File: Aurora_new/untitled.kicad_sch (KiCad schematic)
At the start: 18 parts, among them U15 MCP1826S-5002E/DB, U16 MCP1826S-5002E/DB, U17 MCP1826ST-3302E/DB, U18 MCP1826ST-3302E/DB, U19 MCP1826ST-3302E/DB, U4 MCP1826S-5002E/DB

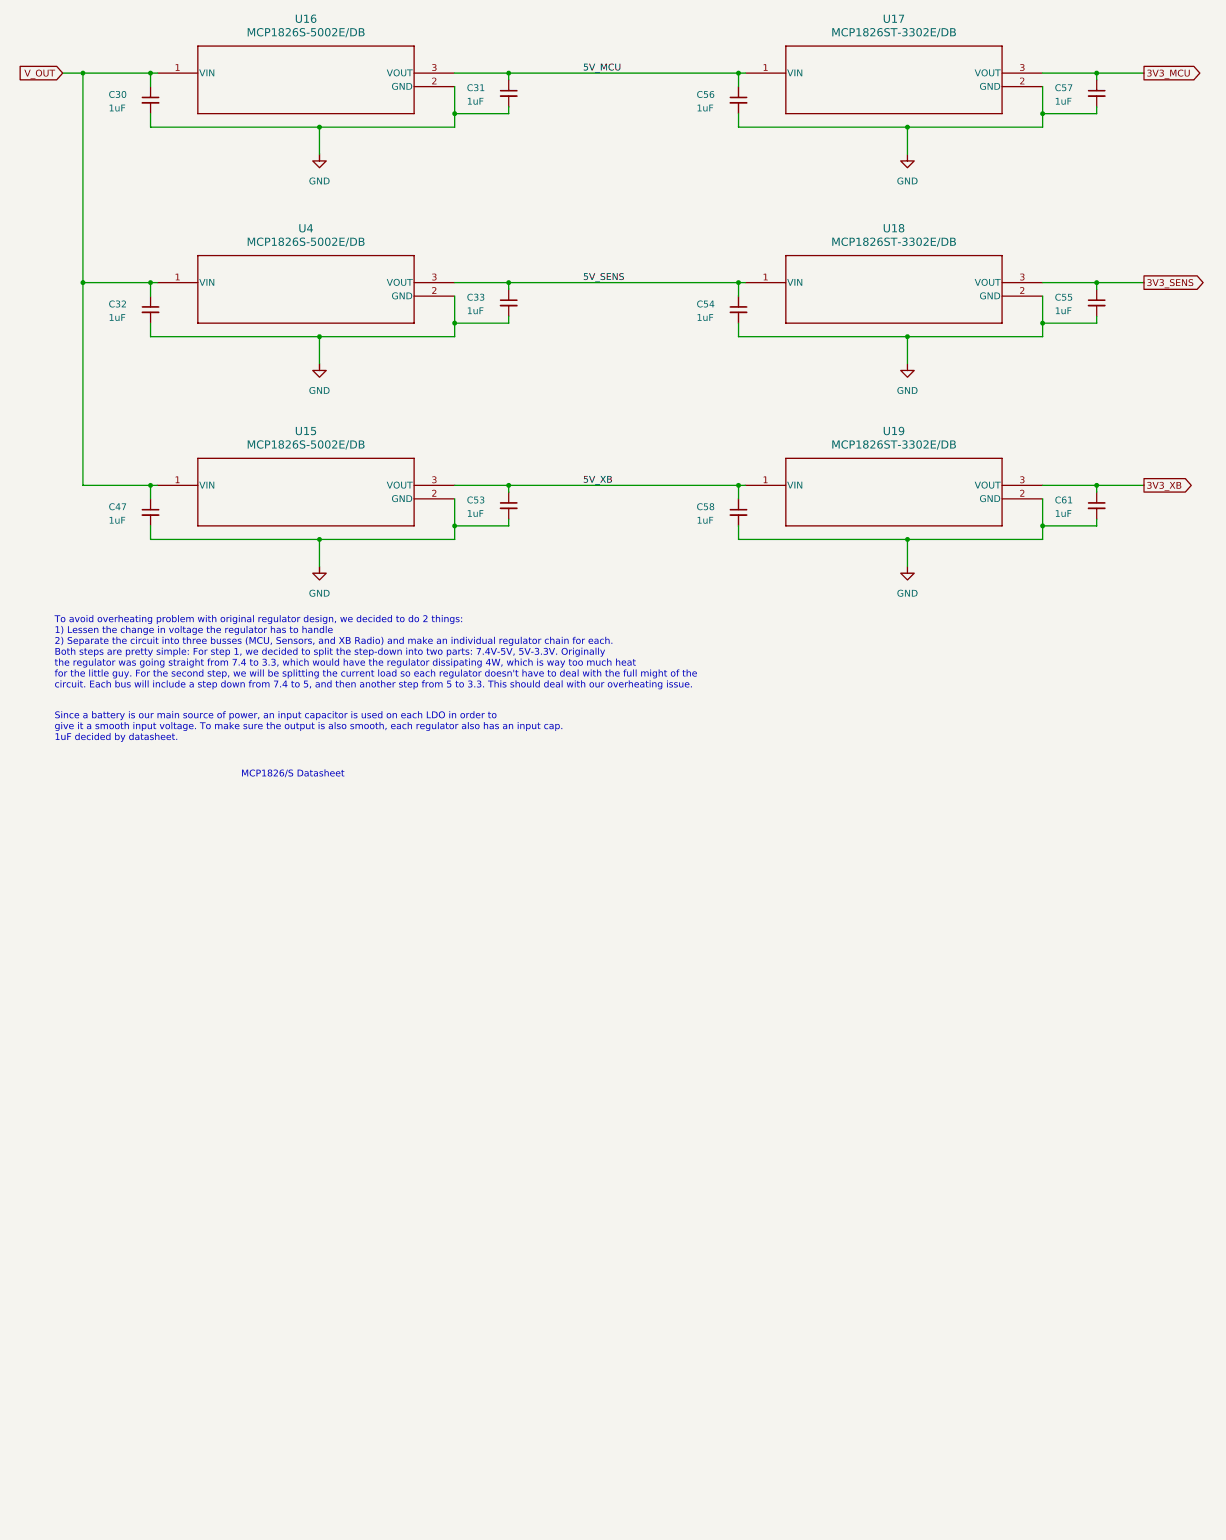
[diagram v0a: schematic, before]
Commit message: regulators mount up
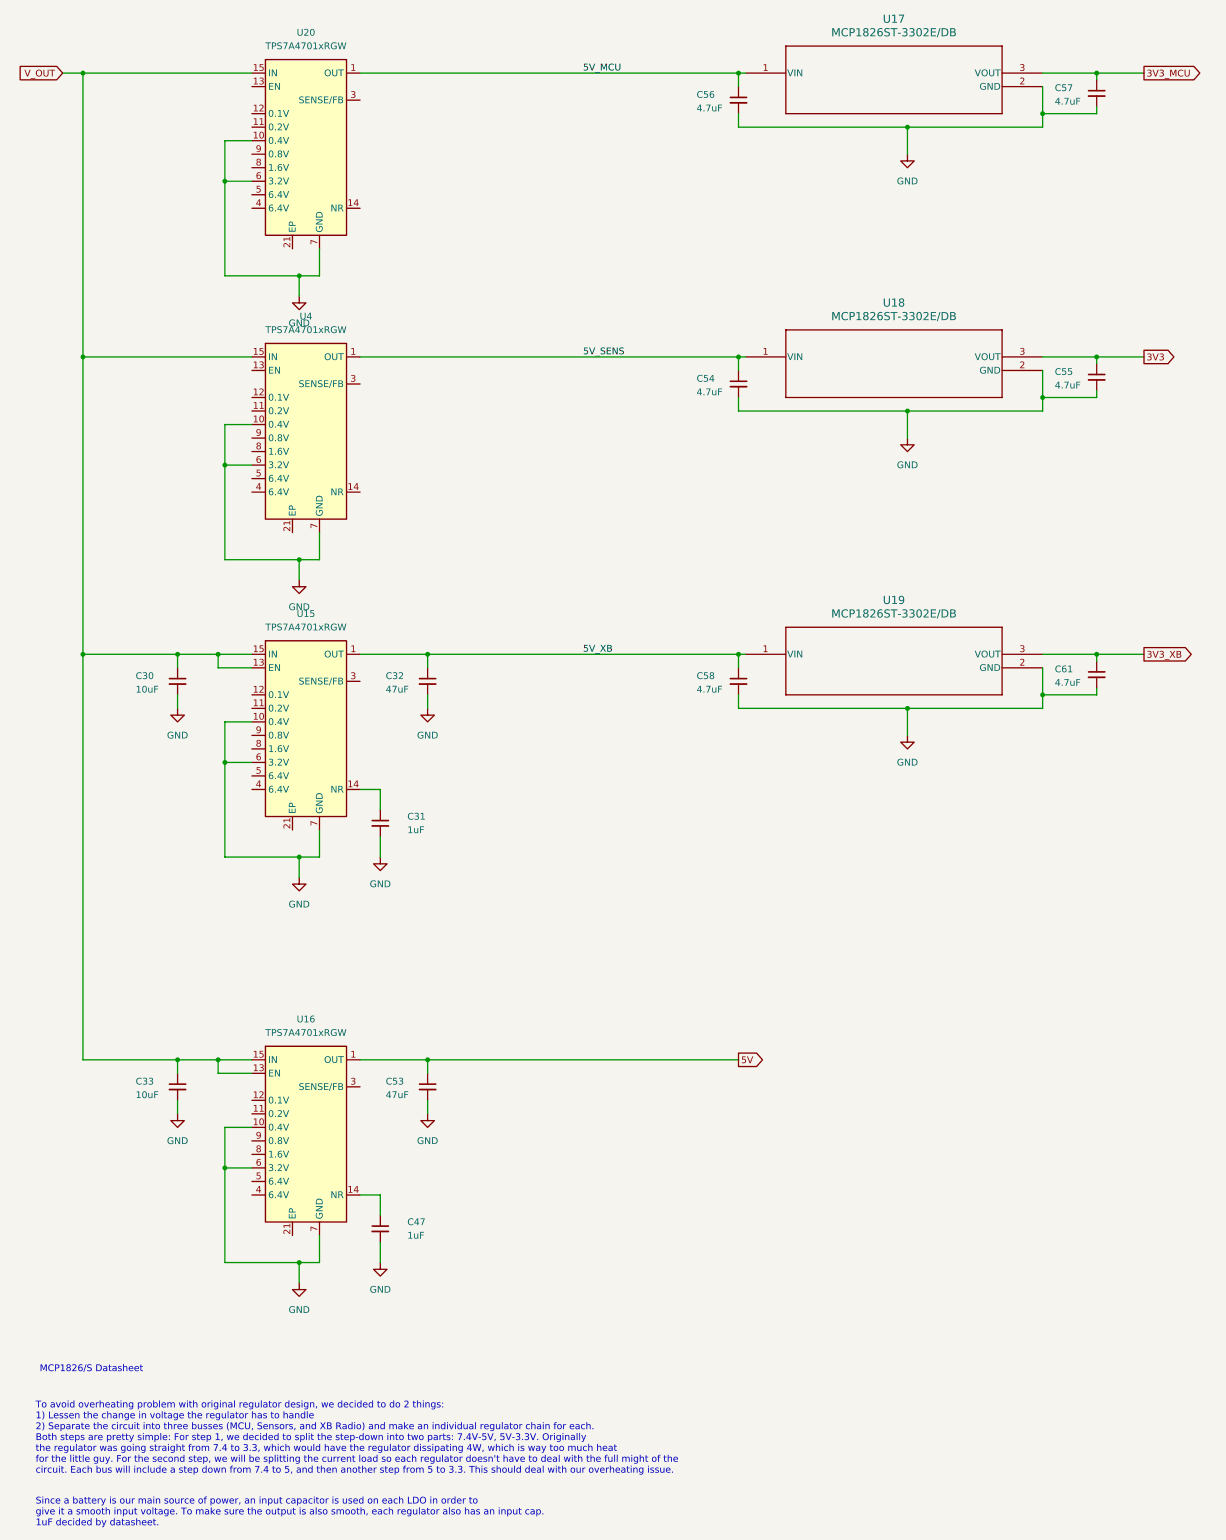
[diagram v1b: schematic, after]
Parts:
- removed U15, U16, U4: MCP1826S-5002E/DB, footprints8:SOT-223_3MC_MCH-L, symbol 2026-01-09_00-59-07:MCP1826S-5002E_DB
- added U15, U16, U20, U4: TPS7A4701xRGW, Package_DFN_QFN:Texas_RGW0020A_VQFN-20-1EP_5x5mm_P0.65mm_EP3.15x3.15mm, symbol Regulator_Linear:TPS7A4701xRGW
- C30, C33: value 1uF -> 10uF
- C32, C53: value 1uF -> 47uF
- C54, C55, C56, C57, C58, C61: value 1uF -> 4.7uF
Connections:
- net 5V_MCU: now also U20.1 (OUT), U20.20 (OUT); no longer C31.1
- net 5V_SENS: now also U4.1 (OUT), U4.20 (OUT); no longer C33.1
- net 5V_XB: now also C32.1, U15.1 (OUT), U15.20 (OUT); no longer C53.1
- net GND: now also U15.10 (0.4V), U15.6 (3.2V), U15.7 (GND), U16.10 (0.4V), U16.6 (3.2V), U16.7 (GND), U20.10 (0.4V), U20.6 (3.2V), U20.7 (GND), U4.10 (0.4V), U4.6 (3.2V), U4.7 (GND)
- net V_OUT: now also C33.1, U15.13 (EN), U15.15 (IN), U15.16 (IN), U16.13 (EN), U16.15 (IN), U16.16 (IN), U20.15 (IN), U20.16 (IN), U4.15 (IN), U4.16 (IN); no longer C32.1, C47.1
- net 3V3_SENS renamed 3V3
- new net: C31.1, U15.14 (NR)
- new net: C47.1, U16.14 (NR)
- new net 5V: C53.1, U16.1 (OUT), U16.20 (OUT)
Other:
- moved on the sheet: C54, C55, C58, C61, U18, U19

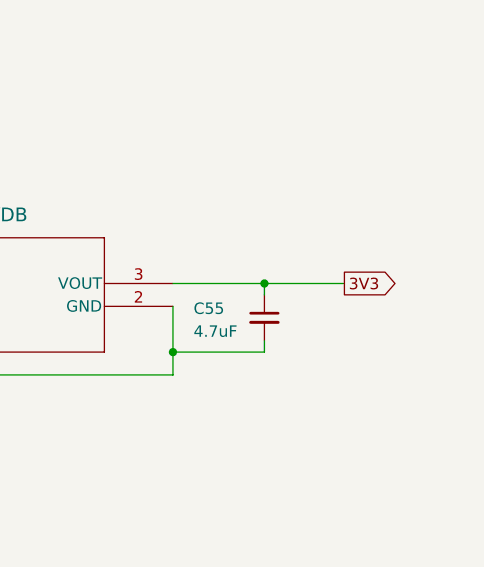
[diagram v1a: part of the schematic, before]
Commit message: bom updates (purchase links, prices, etc) and switching imu because out of stock
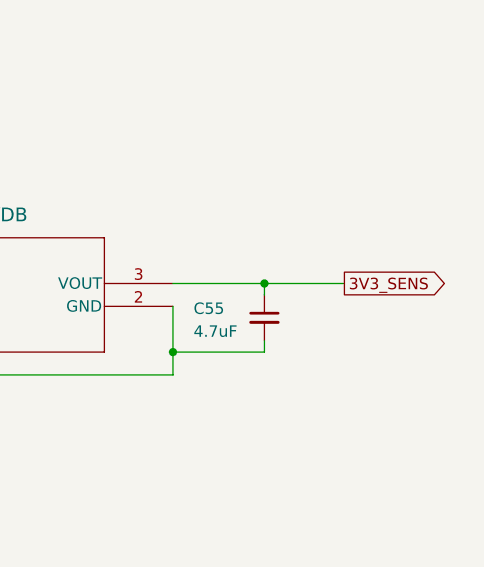
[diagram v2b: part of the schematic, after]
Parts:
- C30, C33: PURCHASE-URL (none) -> https://www.digikey.com/en/products/detail/nextgen-componen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; Price (none) -> $0.17380
- C31, C47: PURCHASE-URL (none) -> https://www.digikey.com/en/products/detail/samsung-electro-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; Price (none) -> $0.08000
- C32, C53: PURCHASE-URL (none) -> https://www.digikey.com/en/products/detail/nextgen-componen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; Price (none) -> $0.44380
- C54, C55, C56, C57, C58, C61: PURCHASE-URL (none) -> https://www.digikey.com/en/products/detail/samsung-electro-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; Price (none) -> $0.34380
- U15, U16, U20, U4: PURCHASE-URL (none) -> https://www.digikey.com/en/products/detail/texas-instrument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; Price (none) -> $5.30000
- U17, U18, U19: PURCHASE-URL (none) -> https://www.digikey.com/en/products/detail/microchip-techno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; Price (none) -> $0.91000
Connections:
- net 3V3 renamed 3V3_SENS

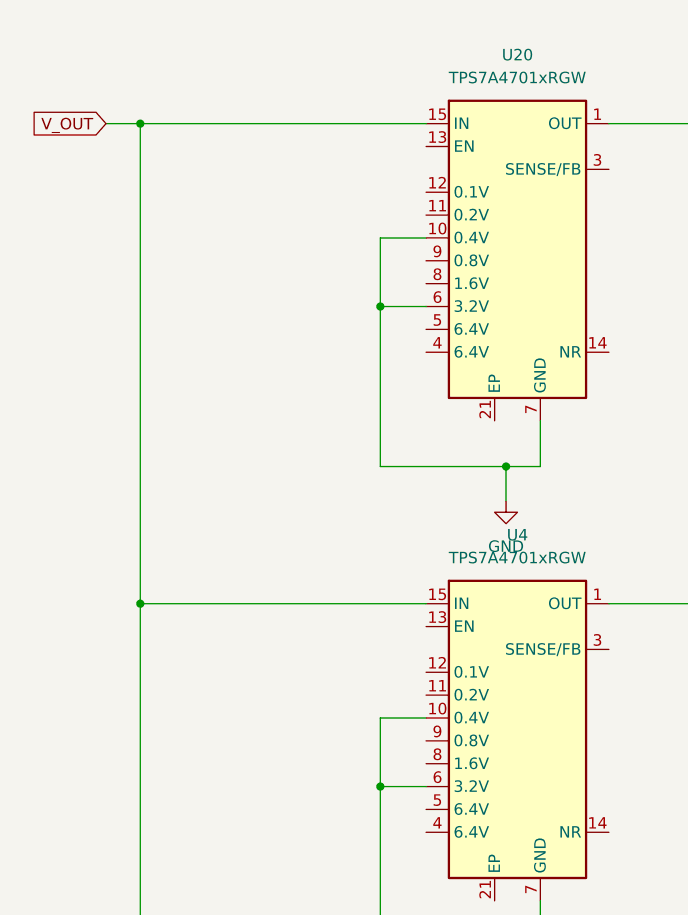
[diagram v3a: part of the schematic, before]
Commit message: continued updating gpios and interrupt pins
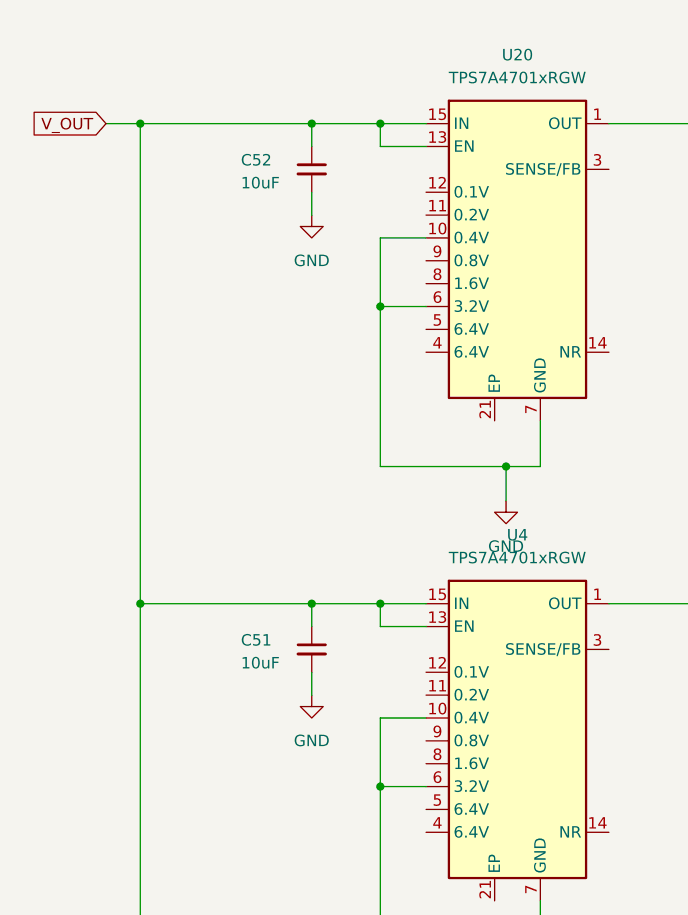
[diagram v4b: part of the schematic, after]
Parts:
- added C51, C52: 10uF, Capacitor_SMD:C_0805_2012Metric, symbol Device:C_Small
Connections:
- net GND: now also C51.2, C52.2
- net V_OUT: now also U20.13 (EN), U4.13 (EN), C51.1, C52.1

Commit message: changes to net labelling
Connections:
- no-connect marks 0 -> 35
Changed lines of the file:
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@@
 		(color 0 0 0 0)
+	)
+	(no_connect
+		(at 59.69 227.33)
+	)
+	(no_connect
+		(at 59.69 110.49)
+	)
+	(no_connect
+		(at 80.01 90.17)
+	)
+	(no_connect
+		(at 80.01 166.37)
+	)
+	(no_connect
+		(at 59.69 57.15)
+	)
+	(no_connect
+		(at 67.31 118.11)
+	)
+	(no_connect
+		(at 59.69 100.33)
+	)
+	(no_connect
+		(at 67.31 64.77)
+	)
+	(no_connect
+		(at 59.69 156.21)
+	)
+	(no_connect
+		(at 80.01 36.83)
+	)
+	(no_connect
+		(at 59.69 41.91)
+	)
+	(no_connect
+		(at 59.69 92.71)
+	)
+	(no_connect
+		(at 59.69 158.75)
+	)
+	(no_connect
+		(at 80.01 146.05)
+	)
+	(no_connect
+		(at 59.69 107.95)
+	)
+	(no_connect
+		(at 59.69 39.37)
+	)
+	(no_connect
+		(at 80.01 57.15)
+	)
+	(no_connect
+		(at 59.69 232.41)
+	)
+	(no_connect
+		(at 59.69 166.37)
+	)
+	(no_connect
+		(at 59.69 224.79)
+	)
+	(no_connect
+		(at 59.69 163.83)
+	)
+	(no_connect
+		(at 59.69 234.95)
+	)
+	(no_connect
+		(at 59.69 95.25)
+	)
+	(no_connect
+		(at 59.69 49.53)
+	)
+	(no_connect
+		(at 59.69 46.99)
+	)
+	(no_connect
+		(at 80.01 222.25)
+	)
+	(no_connect
+		(at 67.31 173.99)
+	)
+	(no_connect
+		(at 59.69 102.87)
+	)
+	(no_connect
+		(at 59.69 54.61)
+	)
+	(no_connect
+		(at 59.69 242.57)
+	)
+	(no_connect
+		(at 59.69 148.59)
+	)
+	(no_connect
+		(at 59.69 240.03)
+	)
+	(no_connect
+		(at 67.31 250.19)
+	)
+	(no_connect
+		(at 80.01 110.49)
+	)
+	(no_connect
+		(at 59.69 151.13)
 	)
 	(wire

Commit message: fixed schematic issues, started organizing components in PCB
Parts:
- removed C33: 10uF, Capacitor_SMD:C_0805_2012Metric, symbol Device:C_Small
- removed C47: 1uF, Capacitor_SMD:C_0805_2012Metric, symbol Device:C_Small
- removed C53: 47uF, Capacitor_SMD:C_0805_2012Metric, symbol Device:C_Small
- removed U16: TPS7A4701xRGW, Package_DFN_QFN:Texas_RGW0020A_VQFN-20-1EP_5x5mm_P0.65mm_EP3.15x3.15mm, symbol Regulator_Linear:TPS7A4701xRGW
- added D9: CD4148W, Diode_SMD:D_0805_2012Metric, symbol Diode:CD4148W
- added LS1: CMT-7525-80-SMT-TR, CMT_7525_80_SMT_TR:XDCR_CMT-7525-80-SMT-TR, symbol CMT-7525-80-SMT-TR:CMT-7525-80-SMT-TR
- added Q9: FMMT619TA, SOT95P237X112-3N, symbol FMMT619TA:FMMT619TA
- added R45: 180, Resistor_SMD:R_0805_2012Metric, symbol Device:R_Small
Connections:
- net 3V3_MCU: now also D9.1 (K), LS1.P
- net GND: now also Q9.2 (E)
- new net: Q9.1 (B), R45.2
- new net: D9.2 (A), LS1.N, Q9.3 (C)
- new net BUZZ: R45.1
- no-connect marks 35 -> 27
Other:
- note added: "BUZZER CIRCUIT"
